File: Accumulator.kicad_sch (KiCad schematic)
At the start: 17 parts, among them J1 1098168, J7 1190363, J8 1190363, K1 AWHSH105D00G, K2 AWHSH105D00G, Q7 PMOS, Q8 NMOS, U4 UCC37324P, U9 MCP4151-xxxx-P

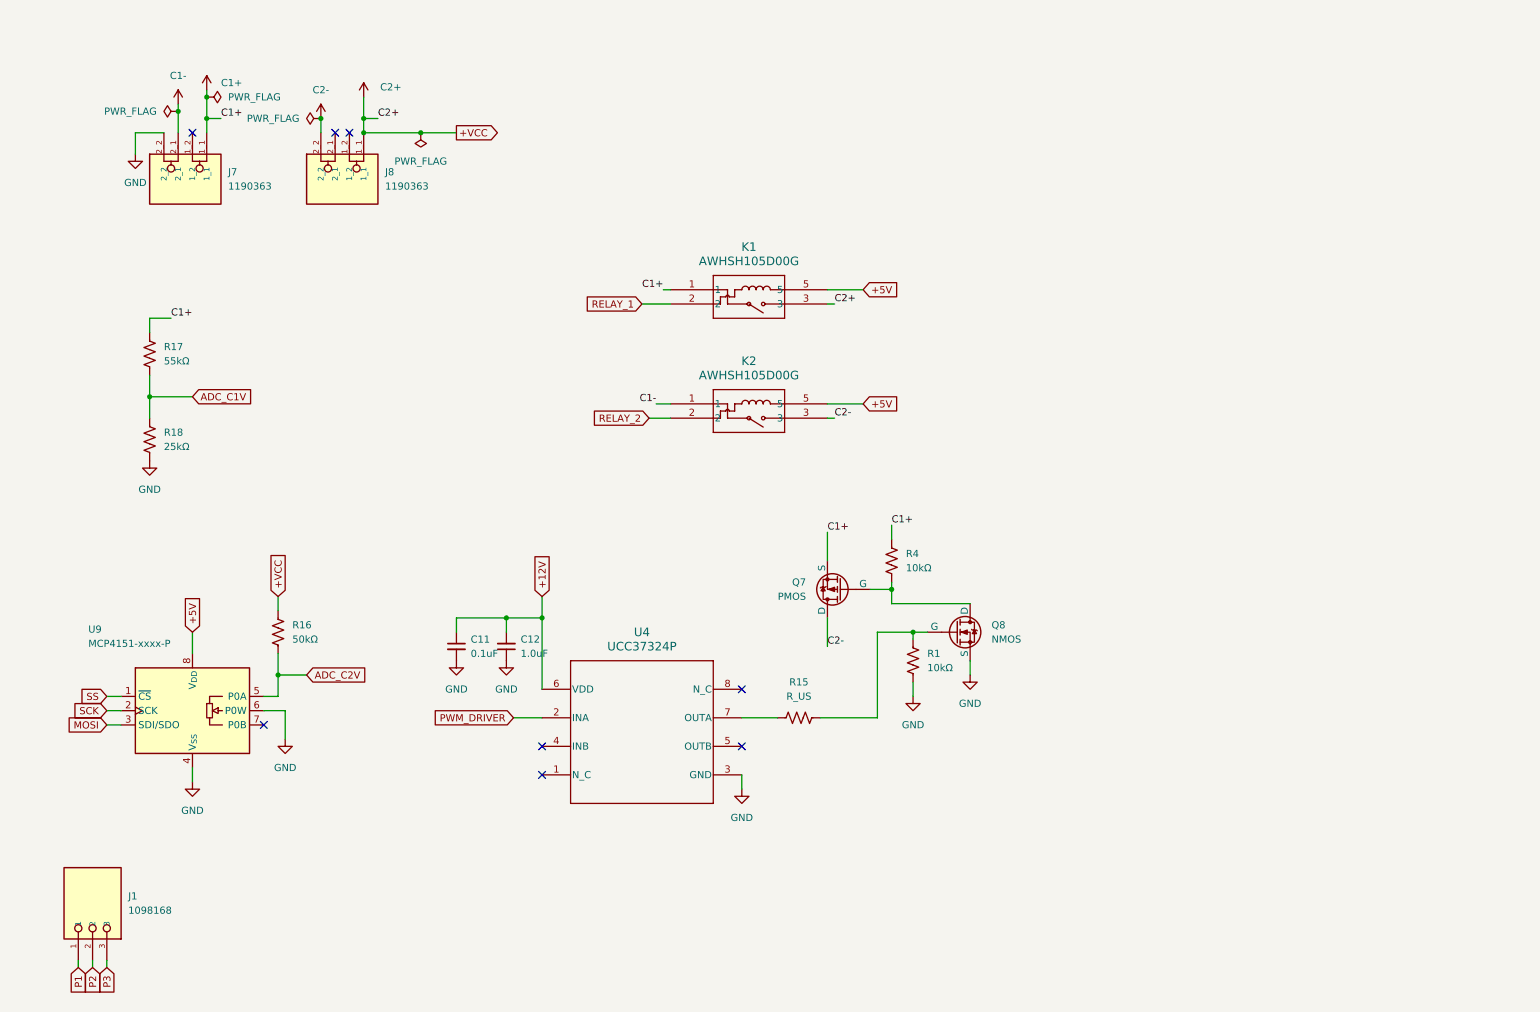
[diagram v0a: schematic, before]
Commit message: Made progress on the PCB, and adressed small issues regarding the schematic
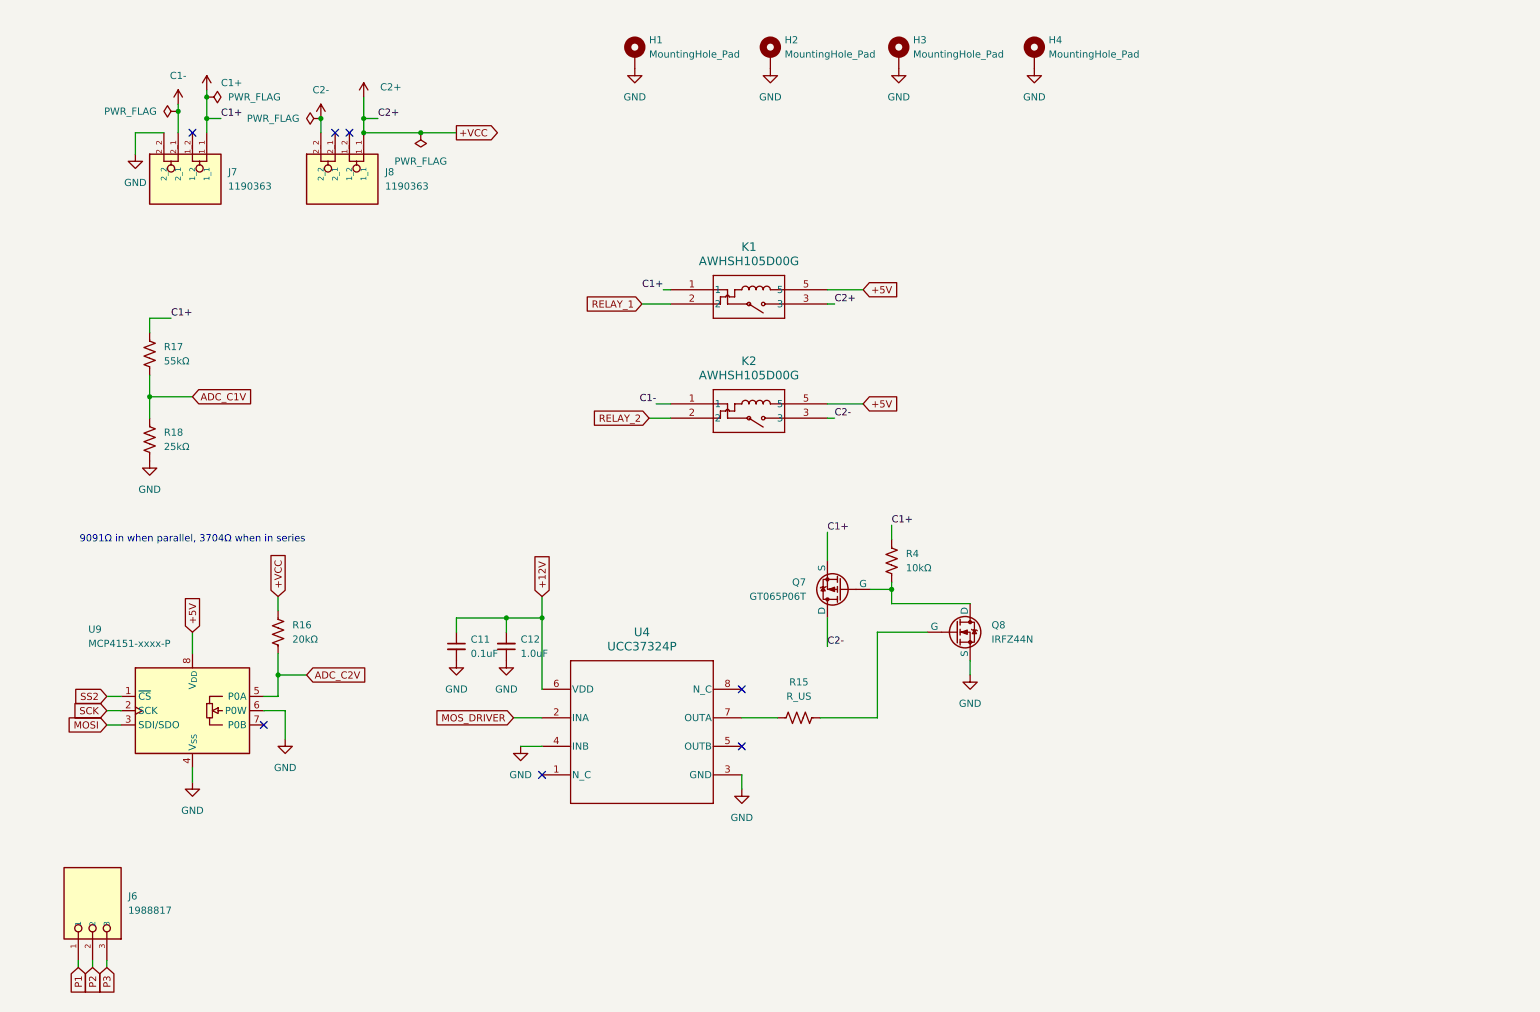
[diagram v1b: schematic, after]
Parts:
- removed J1: 1098168, 1098168:PHOENIX_1098168, symbol Terminal_1098168:1098168
- removed R1: 10kΩ, symbol Device:R_US
- added H1, H2, H3, H4: MountingHole_Pad, MountingHole:MountingHole_3.2mm_M3_DIN965_Pad, symbol Mechanical:MountingHole_Pad
- added J6: 1988817, Terminal_1988817:PHOENIX_1988817, symbol 1988817:1988817
- C11, C12: footprint (none) -> Ceramic_Cap_5.08mm_Spacing:Ceramic_Cap_5.08mm_Spacing
- J7, J8: footprint 1190363:PHOENIX_1190363 -> Terminal_1190363:PHOENIX_1190363
- Q7: value PMOS -> GT065P06T; footprint (none) -> Package_TO_SOT_THT:TO-220-3_Vertical
- Q8: value NMOS -> IRFZ44N; footprint (none) -> Package_TO_SOT_THT:TO-220-3_Vertical
- R15, R17, R18, R4: footprint (none) -> Resistor_THT:R_Axial_DIN0207_L6.3mm_D2.5mm_P10.16mm_Horizontal
- R16: value 50kΩ -> 20kΩ; footprint (none) -> Resistor_THT:R_Axial_DIN0207_L6.3mm_D2.5mm_P10.16mm_Horizontal
- U4: footprint (none) -> Package_DIP:DIP-8_W7.62mm_Socket
- U9: footprint Package_DIP:DIP-8_W7.62mm -> Package_DIP:DIP-8_W7.62mm_Socket
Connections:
- net C2-: now also Q7.2 (D); no longer Q7.1 (D)
- net GND: now also U4.4 (INB), H1.1, H2.1, H3.1, H4.1
- net P1: now also J6.1
- net P2: now also J6.2
- net P3: now also J6.3
- net at R15.2: now also Q8.1 (G); no longer Q8.2 (G)
- net PWM_DRIVER renamed MOS_DRIVER
- net SS renamed SS2
- new net: Q7.1 (G), Q8.2 (D), R4.2
- no-connect marks 8 -> 7
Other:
- note added: "9091Ω in when parallel, 3704Ω when in series"

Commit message: Major design improvements to prototyping PCB
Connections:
- net C1-: no longer K2.1
- net GND: now also K2.1
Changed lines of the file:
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@@
 	(wire
 		(pts
-			(xy 100.33 124.46) (xy 106.68 124.46)
+			(xy 111.76 86.36) (xy 111.76 87.63)
 		)
 		(stroke
@@
 	(wire
 		(pts
-			(xy 46.99 31.75) (xy 46.99 35.56)
+			(xy 100.33 124.46) (xy 106.68 124.46)
 		)
 		(stroke
@@
 	(wire
 		(pts
-			(xy 168.91 118.11) (xy 168.91 119.38)
+			(xy 46.99 31.75) (xy 46.99 35.56)
 		)
 		(stroke
@@
 	(wire
 		(pts
-			(xy 106.68 124.46) (xy 106.68 137.16)
+			(xy 168.91 118.11) (xy 168.91 119.38)
 		)
 		(stroke
@@
 	(wire
 		(pts
-			(xy 127 86.36) (xy 129.54 86.36)
+			(xy 106.68 124.46) (xy 106.68 137.16)
 		)
 		(stroke
@@
 	(wire
 		(pts
+			(xy 111.76 86.36) (xy 129.54 86.36)
+		)
+		(stroke
+			(width 0)
+			(type default)
+		)
+	)
+	(wire
+		(pts
 			(xy 49.53 35.56) (xy 46.99 35.56)
 		)
@@
 		)
 	)
-	(label "C1-"
-		(at 127 86.36 180)
-		(fields_autoplaced yes)
-		(effects
-			(font
-				(size 1.27 1.27)
-			)
-			(justify right bottom)
-		)
-	)
 	(label "C2-"
 		(at 158.75 88.9 0)
@@
 					(unit 1)
 				)
+			)
+		)
+	)
+	(symbol
+		(lib_id "power:GND")
+		(at 111.76 87.63 0)
+		(unit 1)
+		(exclude_from_sim no)
+		(in_bom yes)
+		(on_board yes)
+		(dnp no)
+		(fields_autoplaced yes)
+		(property "Reference" "#PWR056"
+			(at 111.76 93.98 0)
+			(effects
+				(font
+					(size 1.27 1.27)
+				)
+				(hide yes)
+			)
+		)
+		(property "Value" "GND"
+			(at 111.76 92.71 0)
+			(effects
+				(font
+					(size 1.27 1.27)
+				)
+			)
+		)
+		(property "Footprint" ""
+			(at 111.76 87.63 0)
+			(effects
+				(font
+					(size 1.27 1.27)
+				)
+				(hide yes)
+			)
+		)
+		(property "Datasheet" ""
+			(at 111.76 87.63 0)
+			(effects
+				(font
+					(size 1.27 1.27)
+				)
+				(hide yes)
+			)
+		)
+		(property "Description" "Power symbol creates a global label with name \"GND\" , ground"
+			(at 111.76 87.63 0)
+			(effects
+				(font
+					(size 1.27 1.27)
+				)
+				(hide yes)
+			)
+		)
+		(pin "1"
+		)
+		(instances
+			(project "SuperCapacitorBike"
+				(path "/1096cbe7-ac56-48cb-aadd-3e4addcdbbb7/a3002b5e-253f-453a-a6f1-d0dba20d26d3"
+					(reference "#PWR056")
+					(unit 1)
+				)

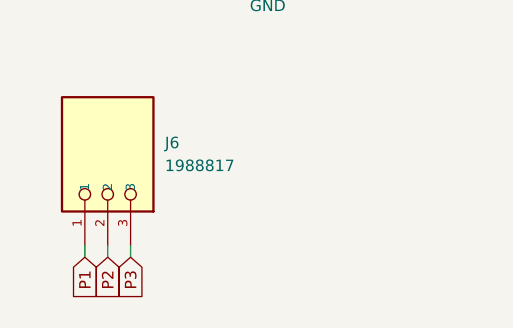
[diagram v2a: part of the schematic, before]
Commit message: Removed a couple redundent VIA's, added +5Vpin
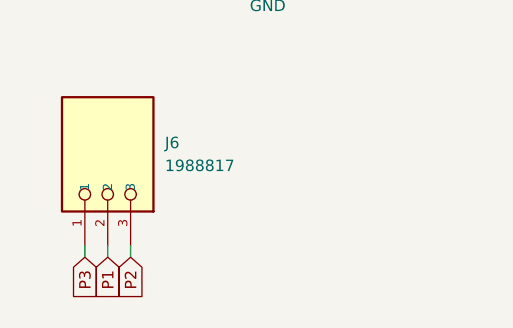
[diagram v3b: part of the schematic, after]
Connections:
- net P1: now also J6.2; no longer J6.1
- net P2: now also J6.3; no longer J6.2
- net P3: now also J6.1; no longer J6.3
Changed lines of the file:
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@@
 		)
 	)
-	(global_label "P3"
+	(global_label "P2"
 		(shape input)
 		(at 29.21 186.69 270)
@@
 		)
 	)
-	(global_label "P2"
+	(global_label "P1"
 		(shape input)
 		(at 26.67 186.69 270)
@@
 		)
 	)
-	(global_label "P1"
+	(global_label "P3"
 		(shape input)
 		(at 24.13 186.69 270)

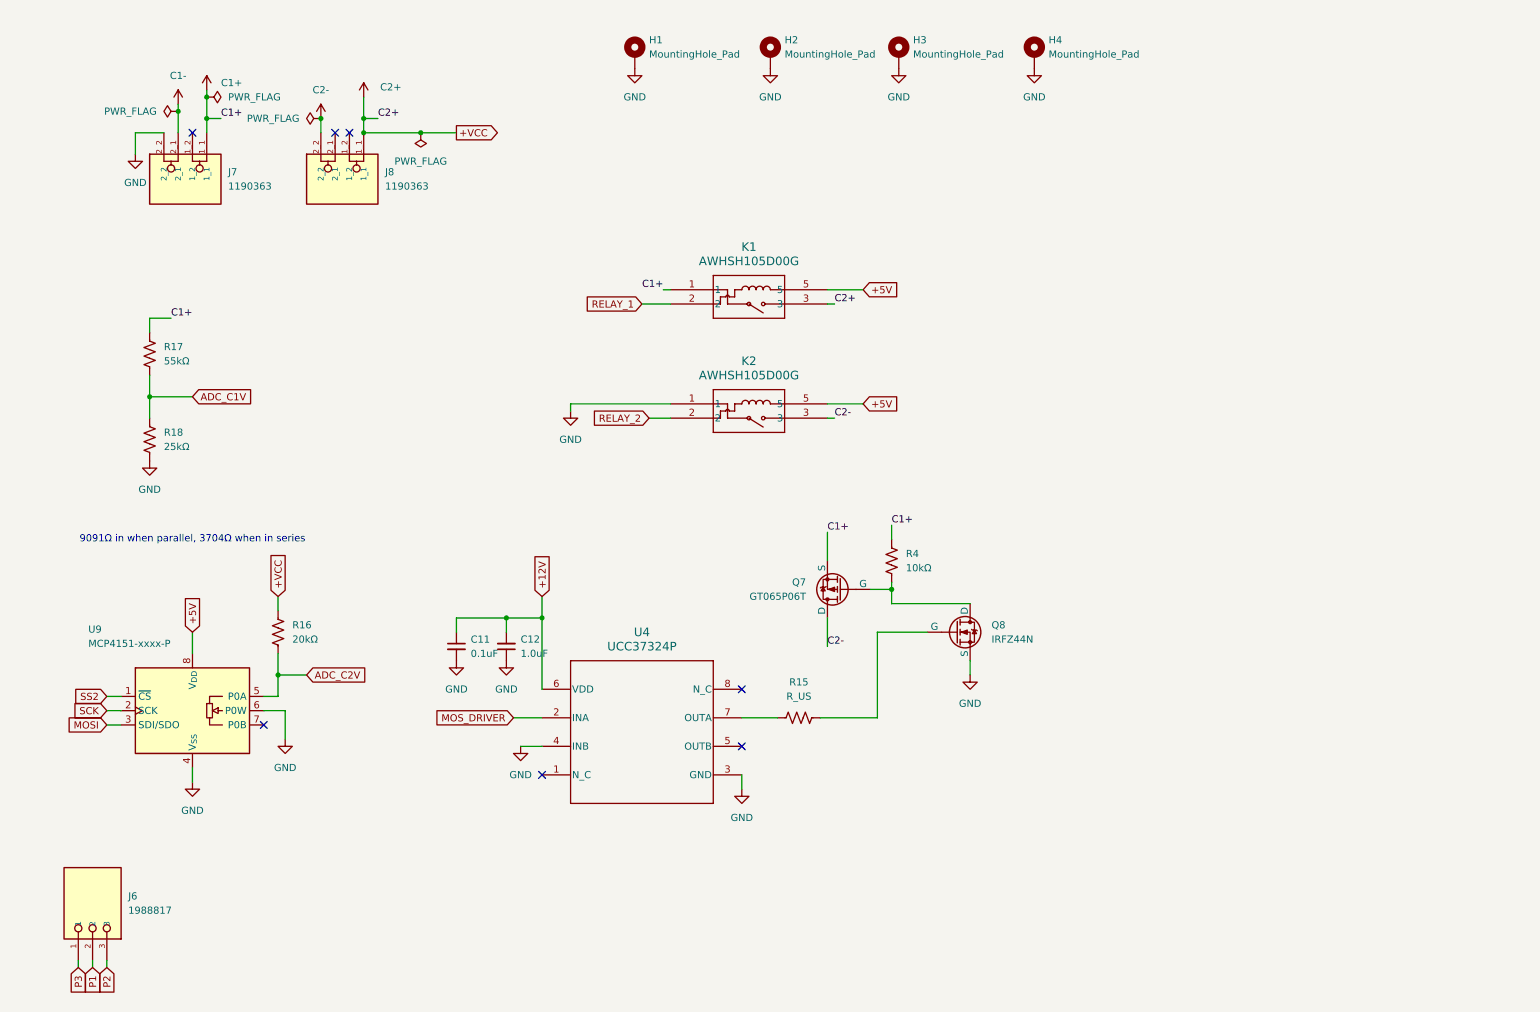
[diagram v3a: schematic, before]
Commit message: Fixed minor inconsistencies, improved orginization, MOSFET gate resistors calculted.
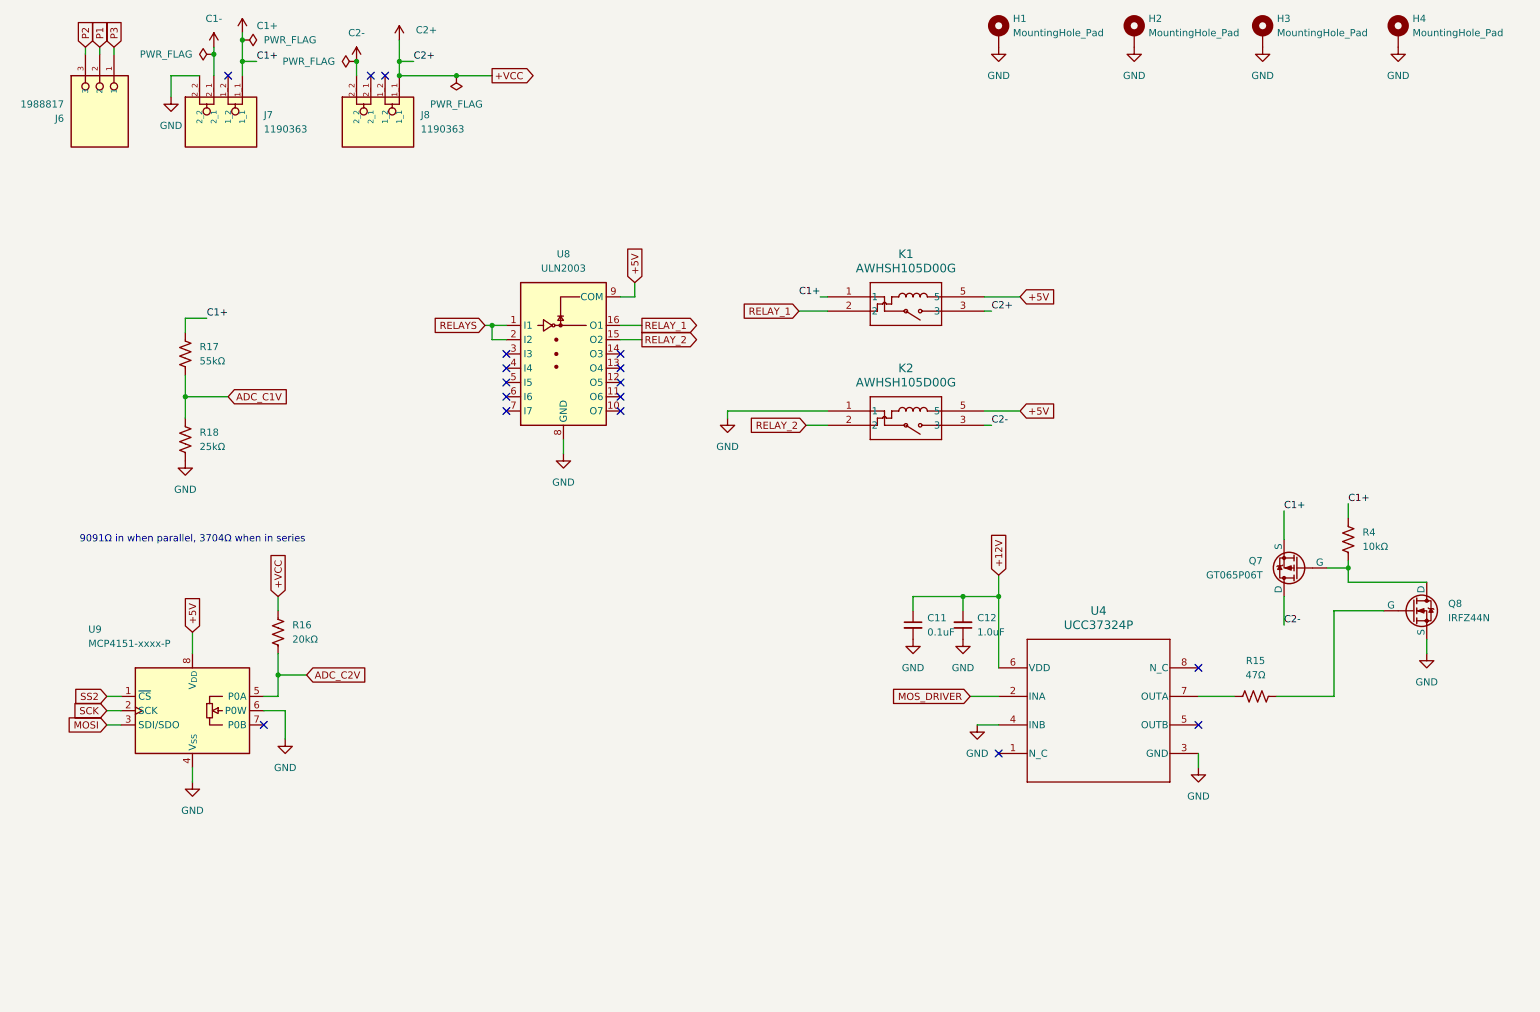
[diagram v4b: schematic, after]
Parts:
- added U8: ULN2003, Package_DIP:DIP-16_W7.62mm_Socket, symbol Transistor_Array:ULN2003
- R15: value R_US -> 47Ω
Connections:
- net +5V: now also U8.9 (COM)
- net GND: now also U8.8 (GND)
- net RELAY_1: now also U8.16 (O1)
- net RELAY_2: now also U8.15 (O2)
- new net RELAYS: U8.1 (I1), U8.2 (I2)
- no-connect marks 7 -> 17
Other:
- moved on the sheet: C11, C12, H1, H2, H3, H4, J6, J7, J8, K1, K2, Q7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

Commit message: Removed alot of redundent VIAs, added testpoints, cleaned up some traces
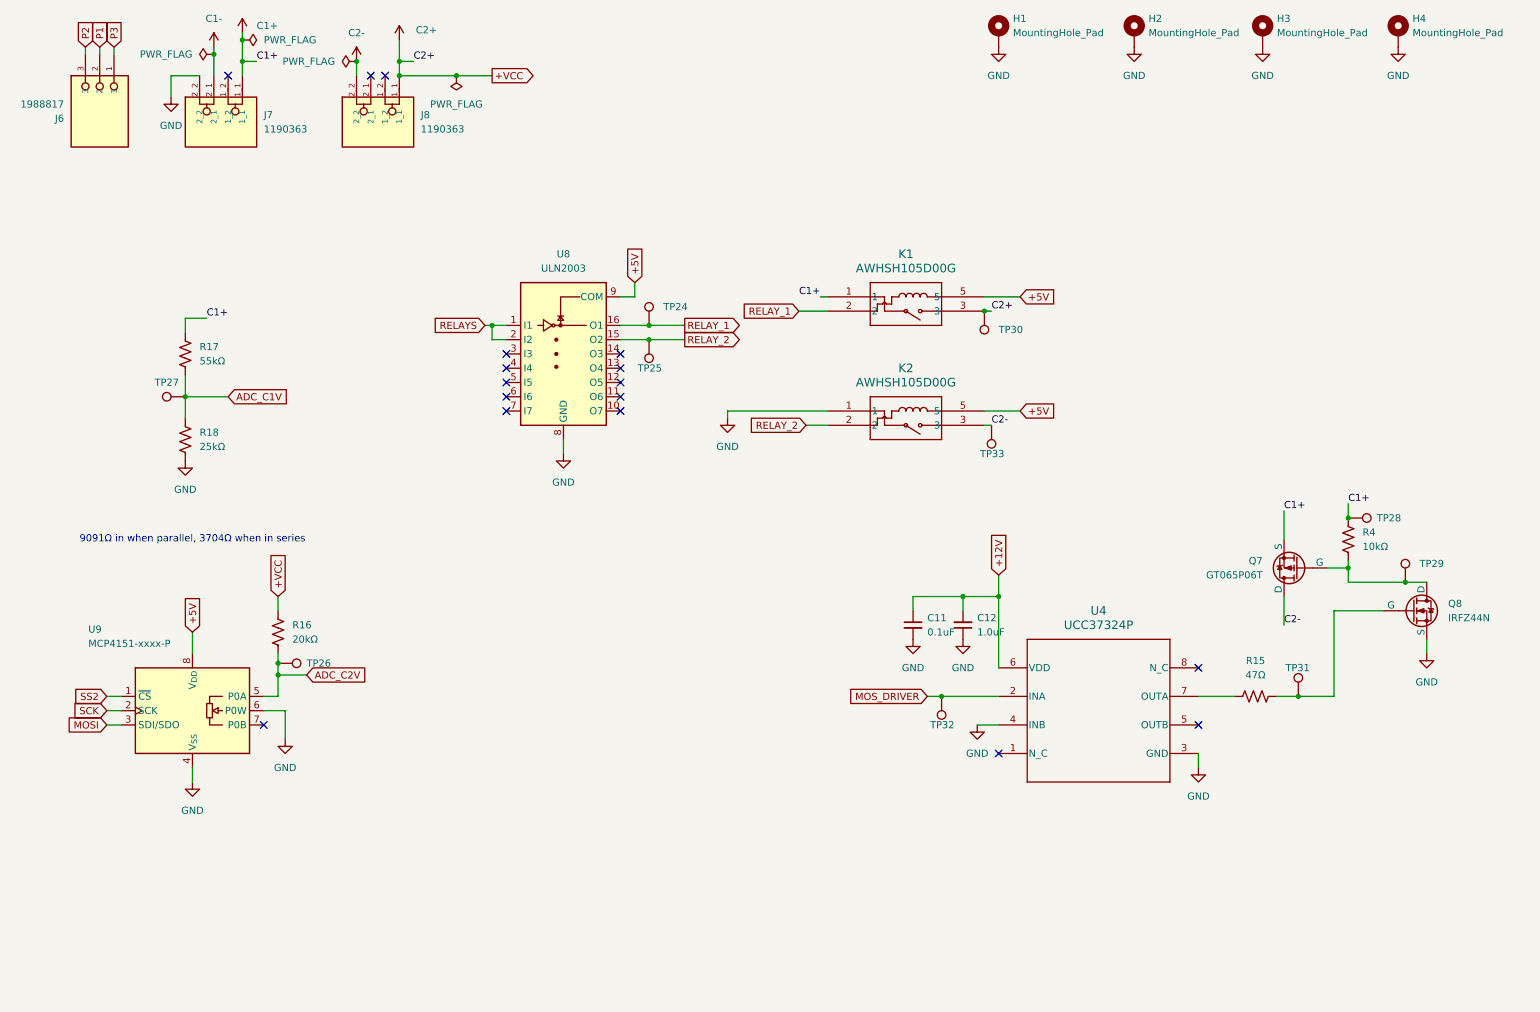
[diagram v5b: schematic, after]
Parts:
- added TP24, TP25, TP26, TP27, TP28, TP29, TP30, TP31, TP32, TP33: TestPoint, TestPoint:TestPoint_THTPad_1.0x1.0mm_Drill0.5mm, symbol Connector:TestPoint
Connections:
- net ADC_C1V: now also TP27.1
- net ADC_C2V: now also TP26.1
- net C1+: now also TP28.1
- net C2+: now also TP30.1
- net C2-: now also TP33.1
- net MOS_DRIVER: now also TP32.1
- net RELAY_1: now also TP24.1
- net RELAY_2: now also TP25.1
- net at Q8.1 (G), R15.2: now also TP31.1
- net at Q7.1 (G), Q8.2 (D), R4.2: now also TP29.1
